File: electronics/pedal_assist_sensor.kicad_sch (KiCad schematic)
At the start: 10 parts, among them J2 Conn_01x05, U1 ATtiny824-X, U2 DRV505x, U3 DRV505x, U4 TLV70033_SOT23-5

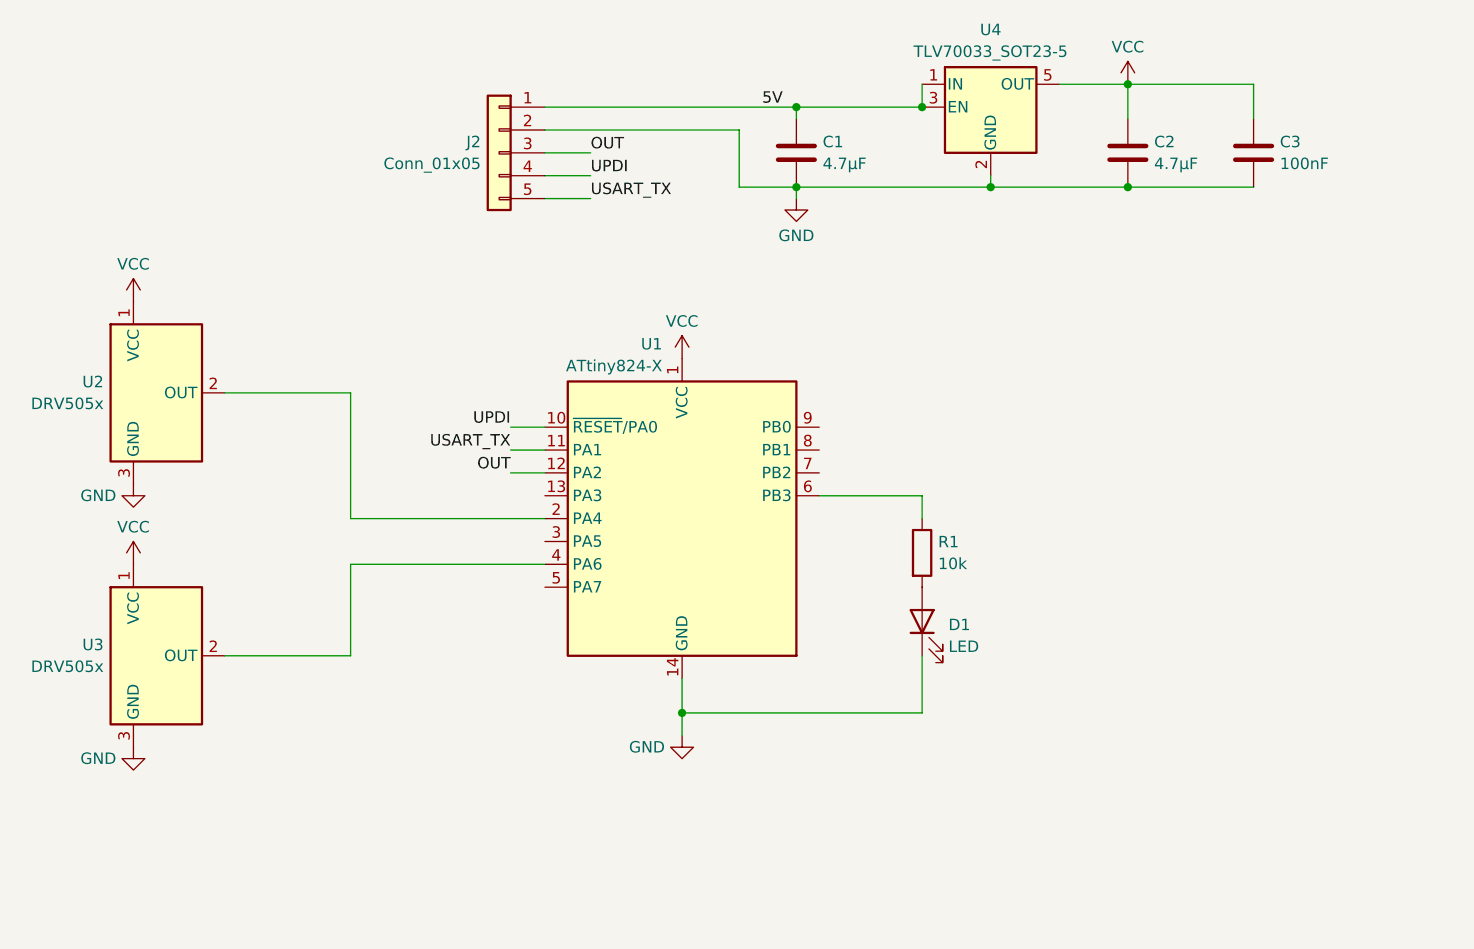
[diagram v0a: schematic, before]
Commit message: Updates for publication, add images
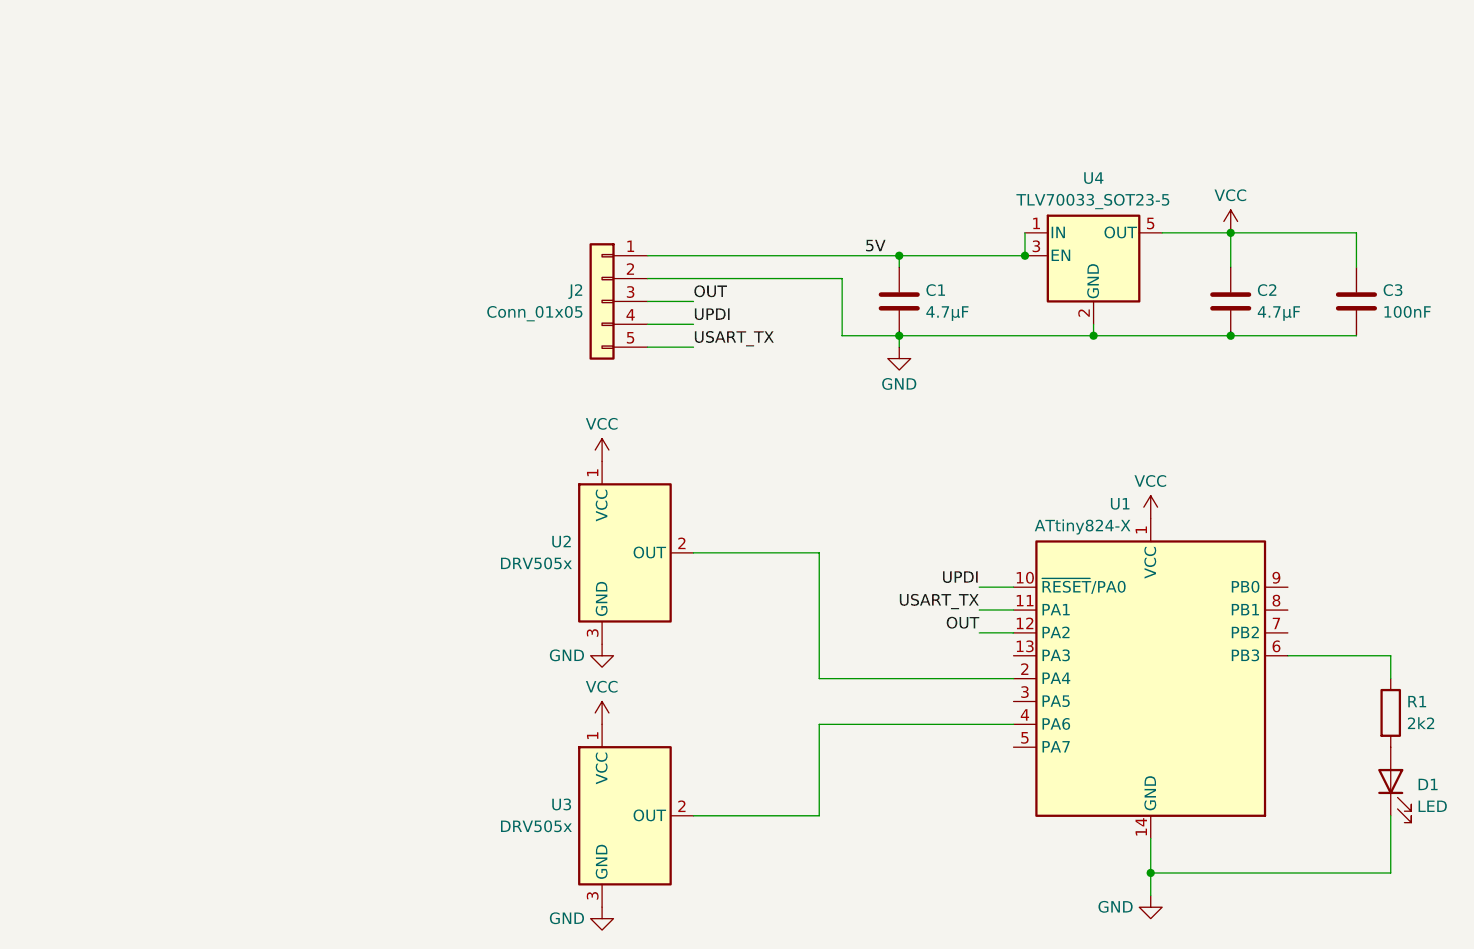
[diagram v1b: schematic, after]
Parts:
- R1: value 10k -> 2k2
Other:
- moved on the sheet: C1, C2, C3, D1, J2, R1, U1, U2, U3, U4
